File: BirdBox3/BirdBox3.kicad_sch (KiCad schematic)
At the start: 23 parts, among them J1 Raspberry Pi 2x20 Conn, J2 1x2 female, J2b 1x2 male, J3 JST, J4 1x6 female, J4 1x6 male, M1 Raspberry Pi Pico, M2 Wide-input Shim

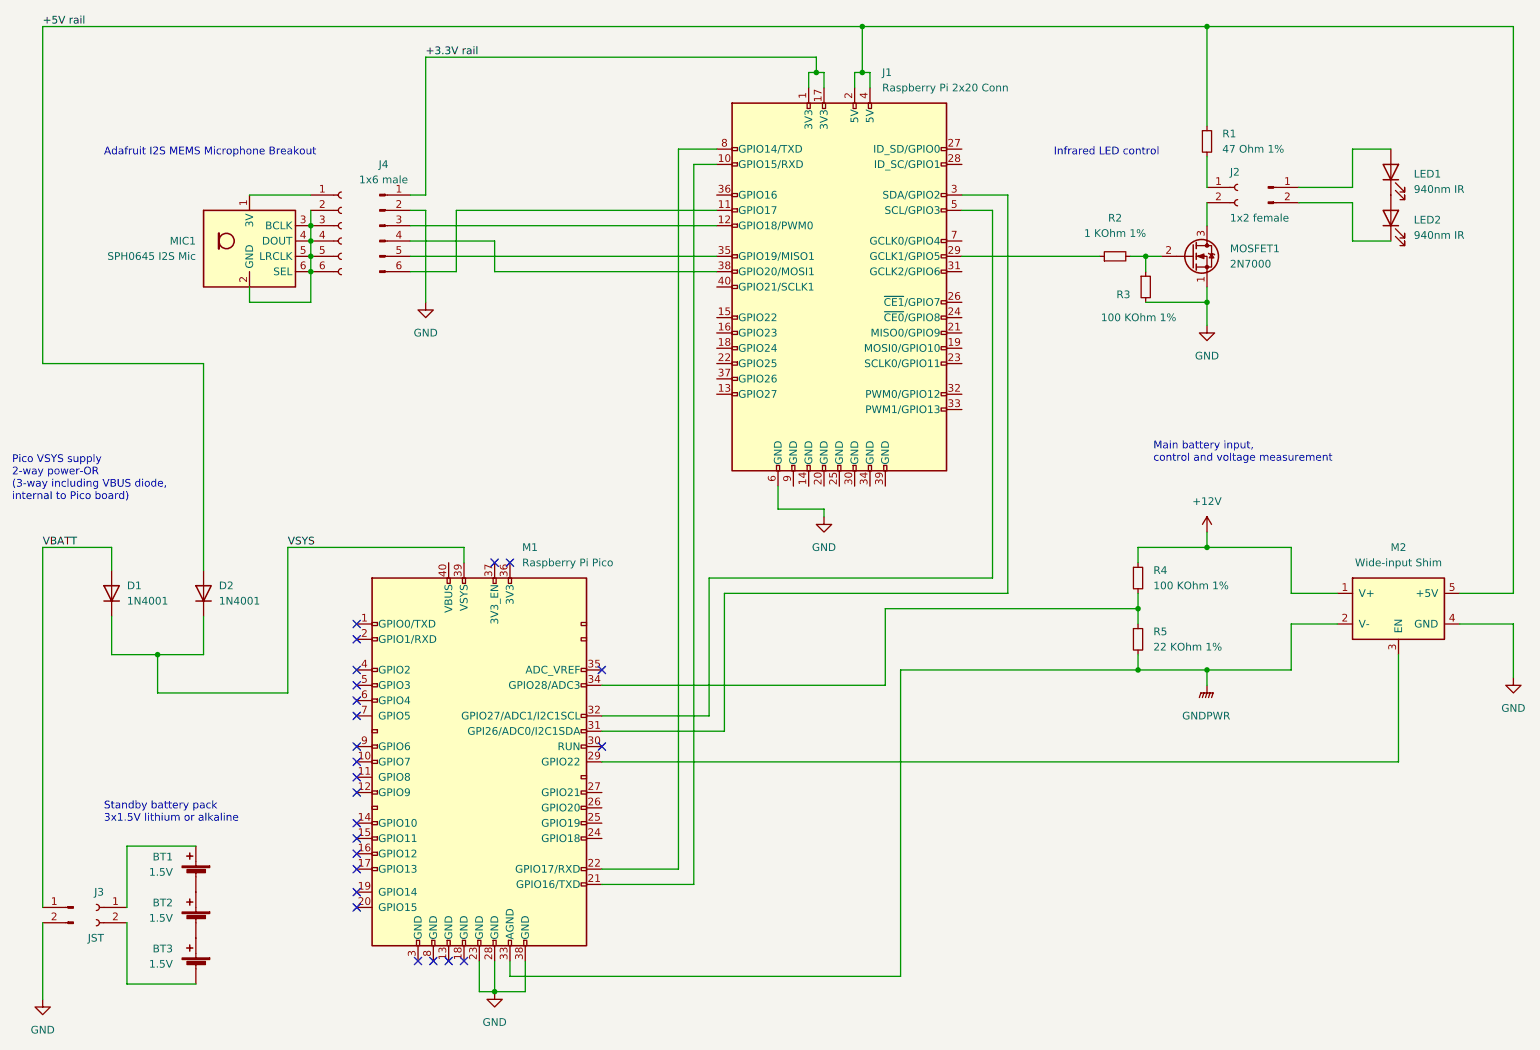
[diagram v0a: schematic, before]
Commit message: Updates to reflect the actual BirdBox3 build of 2023
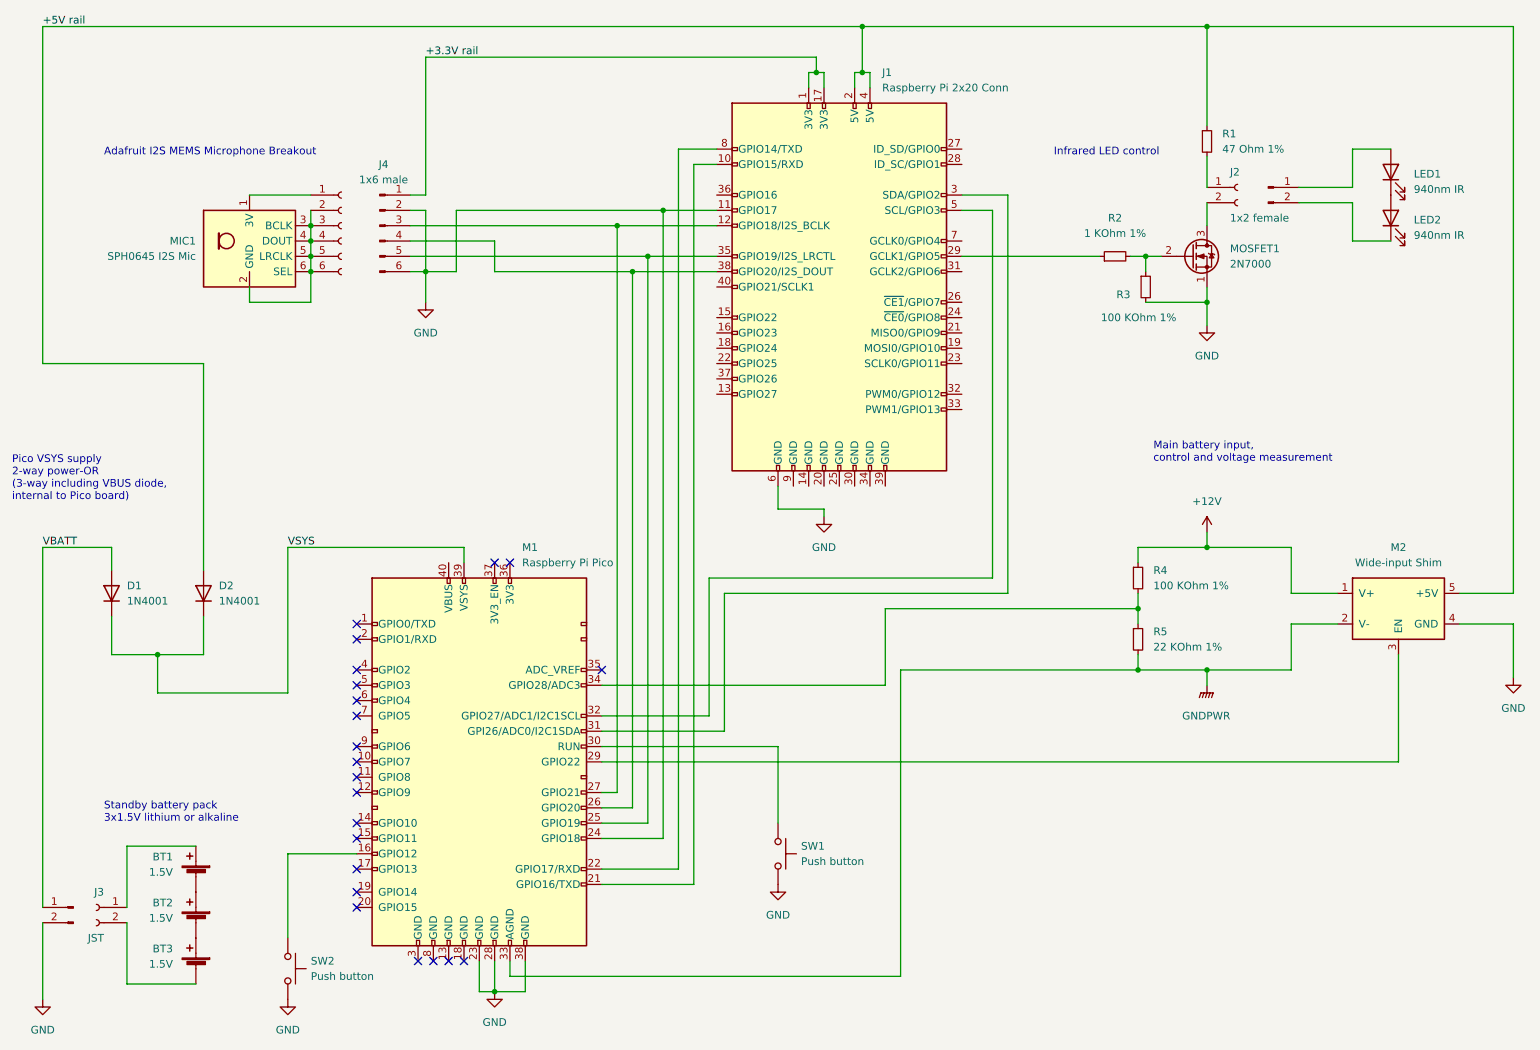
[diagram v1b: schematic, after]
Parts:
- added SW1, SW2: Push button, symbol Switch:SW_Push
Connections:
- net GND: now also J1.11 (GPIO17), J4.6 (Pin_6), M1.24 (GPIO18), SW1.2, SW2.2
- net at J1.12 (GPIO18/I2S_BCLK), J4.3 (Pin_3): now also M1.27 (GPIO21)
- net at J1.35 (GPIO19/I2S_LRCTL), J4.5 (Pin_5): now also M1.25 (GPIO19)
- net at J1.38 (GPIO20/I2S_DOUT), J4.4 (Pin_4): now also M1.26 (GPIO20)
- net at M1.16 (GPIO12): now also SW2.1
- net at M1.30 (RUN): now also SW1.1
- no-connect marks 24 -> 22
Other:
- title: BirdBox3 Interface Hat for Pi Zero 2 W -> BirdBox3 Interface Hatlet for Pi Zero W

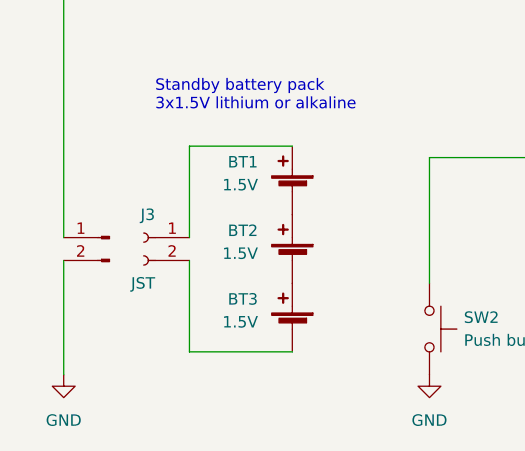
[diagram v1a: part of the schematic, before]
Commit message: 2024 version, with batt terminal block instead of JST connector
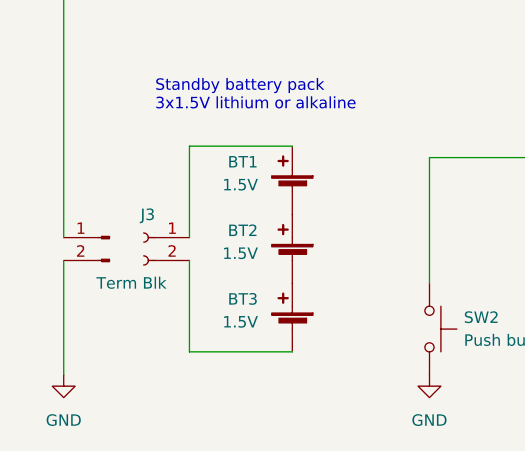
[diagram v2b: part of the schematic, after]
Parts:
- J3: value JST -> Term Blk
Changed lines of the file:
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@@
     (date "2024-02-02")
     (rev "1.0")
+    (comment 1 "2024 version")
   )
   (junction (at 90.17 63.5) (diameter 0) (color 0 0 0 0)
@@
       (effects (font (size 1.27 1.27)) (justify left))
     )
-    (property "Value" "JST" (id 1) (at 36.83 173.99 0)
+    (property "Value" "Term Blk" (id 1) (at 38.1 173.99 0)
       (effects (font (size 1.27 1.27)) (justify left))
     )
@@
     )
     (path "/0f728f4f-92f1-468c-8943-d5388d111303"
-      (reference "J3") (unit 1) (value "JST") (footprint "")
+      (reference "J3") (unit 1) (value "Term Blk") (footprint "")
     )
     (path "/1b524548-72e1-44f9-805f-3e0c5799fd28"

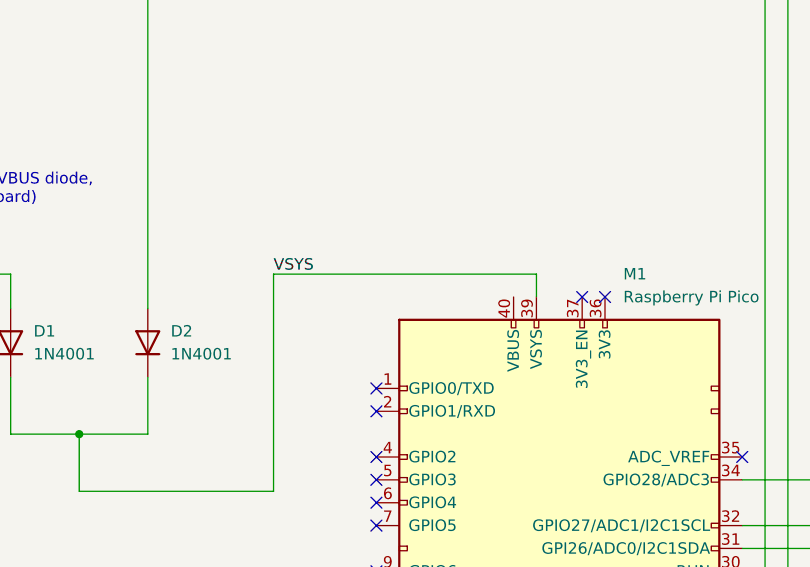
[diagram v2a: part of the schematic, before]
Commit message: Added connection between Pico VBAT and VSYS - deliberately shorted together
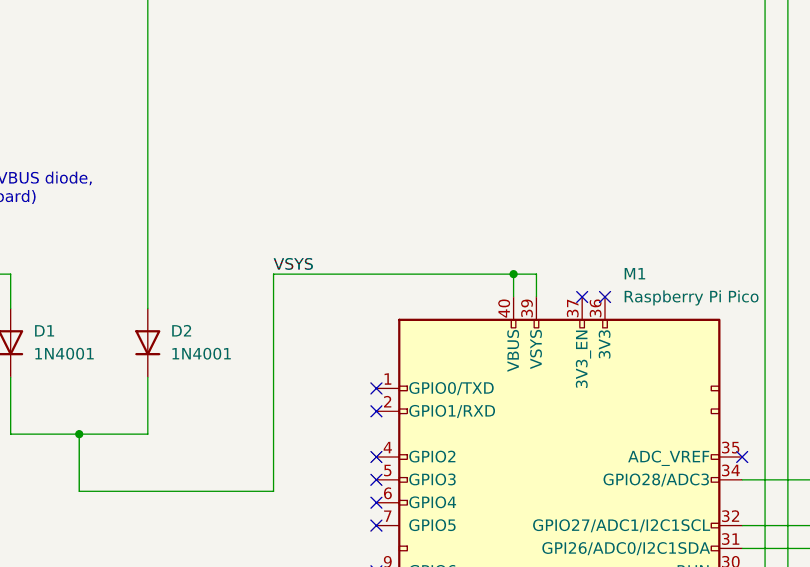
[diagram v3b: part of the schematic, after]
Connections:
- net VSYS: now also M1.40 (VBUS)
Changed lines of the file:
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@@
   (junction (at 129.54 53.34) (diameter 0) (color 0 0 0 0)
+  )
+  (junction (at 93.98 109.22) (diameter 0) (color 0 0 0 0)
   )
   (junction (at 209.55 60.96) (diameter 0) (color 0 0 0 0)
@@
     (stroke (width 0) (type default) (color 0 0 0 0))
   )
+  (wire (pts (xy 93.98 109.22) (xy 93.98 111.76))
+    (stroke (width 0) (type default) (color 0 0 0 0))
+  )
   (wire (pts (xy 233.68 116.84) (xy 241.3 116.84))
     (stroke (width 0) (type default) (color 0 0 0 0))
@@
     (stroke (width 0) (type default) (color 0 0 0 0))
   )
+  (wire (pts (xy 93.98 109.22) (xy 96.52 109.22))
+    (stroke (width 0) (type default) (color 0 0 0 0))
+  )
   (wire (pts (xy 119.38 144.78) (xy 251.46 144.78))
     (stroke (width 0) (type default) (color 0 0 0 0))
@@
     (stroke (width 0) (type default) (color 0 0 0 0))
   )
-  (wire (pts (xy 67.31 109.22) (xy 96.52 109.22))
-    (stroke (width 0) (type default) (color 0 0 0 0))
-  )
+  (wire (pts (xy 67.31 109.22) (xy 93.98 109.22))
+    (stroke (width 0) (type default) (color 0 0 0 0))
+  )

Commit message: Recent changes to 2025 versions
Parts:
- removed BT1, BT2, BT3: 1.5V, symbol Device:Battery_Cell
- removed D1, D2: 1N4001, Diode_THT:D_DO-41_SOD81_P10.16mm_Horizontal, symbol Diode:1N4001
- removed J3: Term Blk, symbol Connector:Conn_01x02_Female
- removed J?: JST, symbol Connector:Conn_01x02_Male
- removed SW2: Push button, symbol Switch:SW_Push
- M1: value Raspberry Pi Pico -> Pimoroni Pico Lipo 4MB
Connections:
- net +5V rail: now also M1.40 (VBUS)
- net VSYS: no longer names the net of M1.39 (VSYS)
- net VSYS: no longer M1.40 (VBUS)
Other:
- note removed: "Pico VSYS supply 2-way power-OR (3-way including VBUS diode, internal to Pico board)"
- note removed: "Standby battery pack 3x1.5V lithium or alkaline"
